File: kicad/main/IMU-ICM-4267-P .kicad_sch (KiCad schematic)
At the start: 7 parts, among them U19 ICM-42607-P

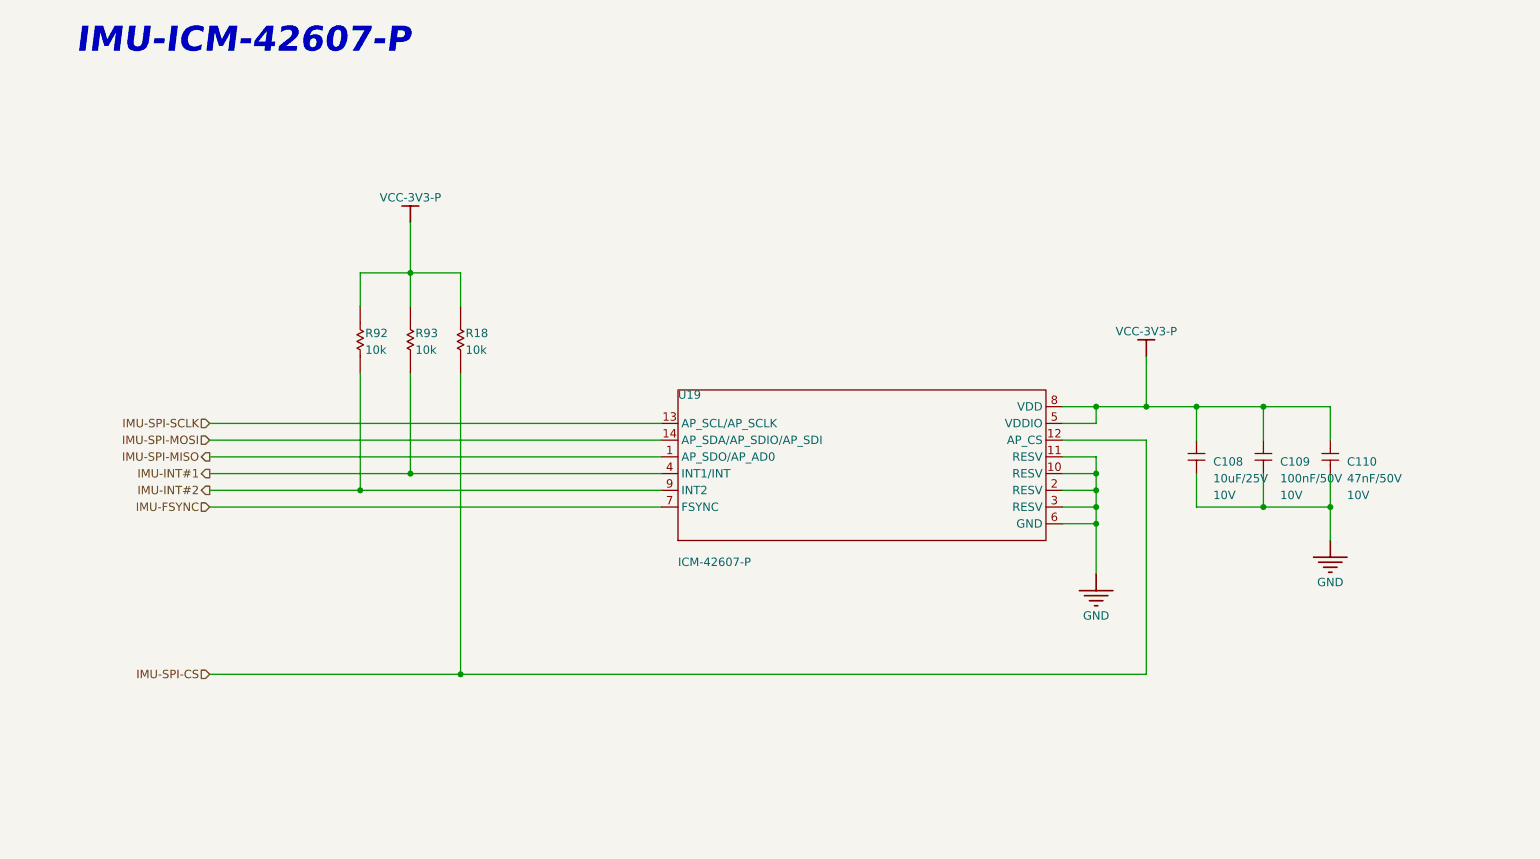
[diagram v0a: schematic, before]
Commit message: Cliff/bumpers connector
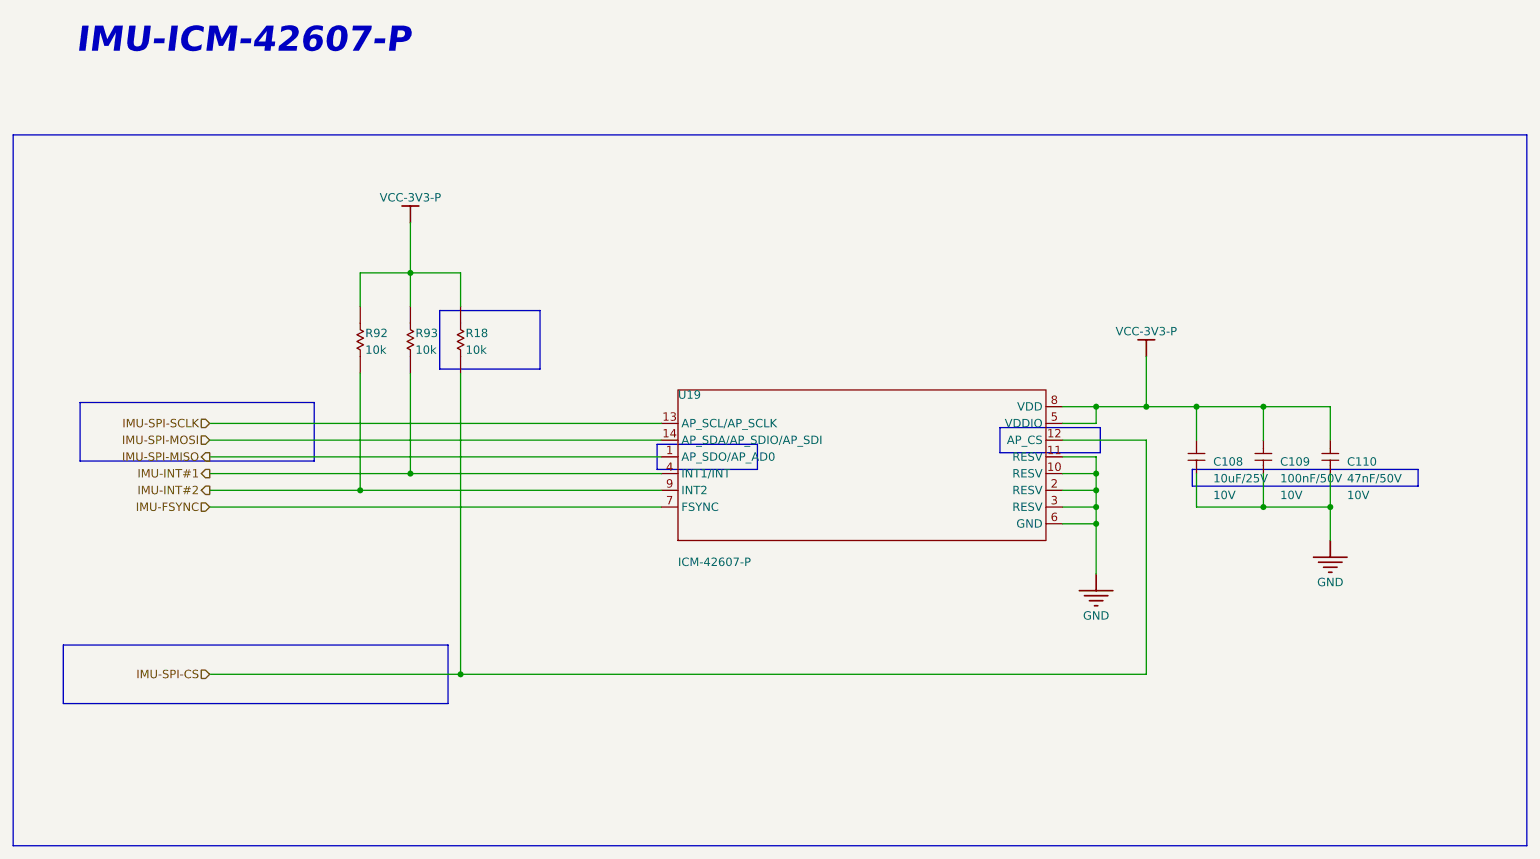
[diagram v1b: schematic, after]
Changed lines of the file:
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@@
 	(generator_version "10.0")
 	(paper "A2")
+	(rectangle
+		(start 199.39 194.31)
+		(end 234.95 203.2)
+		(stroke
+			(width 0)
+			(type solid)
+		)
+		(fill
+			(type color)
+			(color 72 0 0 1)
+		)
+	)
+	(rectangle
+		(start 196.85 231.14)
+		(end 255.27 240.03)
+		(stroke
+			(width 0)
+			(type solid)
+		)
+		(fill
+			(type color)
+			(color 72 0 0 1)
+		)
+	)
+	(rectangle
+		(start 368.3 204.47)
+		(end 402.59 207.01)
+		(stroke
+			(width 0)
+			(type solid)
+		)
+		(fill
+			(type color)
+			(color 72 0 0 1)
+		)
+	)
+	(rectangle
+		(start 339.09 198.12)
+		(end 354.33 201.93)
+		(stroke
+			(width 0)
+			(type solid)
+		)
+		(fill
+			(type color)
+			(color 72 0 0 1)
+		)
+	)
+	(rectangle
+		(start 254 180.34)
+		(end 269.24 189.23)
+		(stroke
+			(width 0)
+			(type solid)
+		)
+		(fill
+			(type color)
+			(color 72 0 0 1)
+		)
+	)
+	(rectangle
+		(start 287.02 200.66)
+		(end 302.26 204.47)
+		(stroke
+			(width 0)
+			(type solid)
+		)
+		(fill
+			(type color)
+			(color 72 0 0 1)
+		)
+	)
+	(rectangle
+		(start 189.23 153.67)
+		(end 419.1 261.62)
+		(stroke
+			(width 0)
+			(type solid)
+		)
+		(fill
+			(type color)
+			(color 0 72 0 1)
+		)
+	)
 	(text "IMU-ICM-42607-P"
 		(exclude_from_sim no)

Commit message: Second review round
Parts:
- added R72: 10k, Resistor_SMD:R_0603_1608Metric, symbol DesignLibrary:IMU_3_Resistor-1_DesignLibrary.SchLib
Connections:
- net IMU-SPI-MOSI is gone; now on net IMU-SDA: U19.14 (AP_SDA/AP_SDIO/AP_SDI)
- net VCC-3V3-P: now also U19.12 (AP_CS), R72.1
- net IMU-SPI-CS renamed IMU-SDA
- net IMU-SDA: no longer U19.12 (AP_CS)
- net IMU-SPI-MISO: no longer names the net of U19.1 (AP_SDO/AP_AD0)
- net IMU-SPI-SCLK renamed IMU-SCL
- net IMU-SCL: now also R72.2
- no-connect marks 0 -> 1

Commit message: STM32 power rail switch
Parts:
- C108: value 10uF/25V -> 10uF/6.3V; LCSC C96446 -> C1691; VOLTAGERATE 10V -> (none)
- C109: value 100nF/50V -> 100nF/6.3V; LCSC C1591 -> C5356672; VOLTAGERATE 10V -> (none)
- C110: LCSC (none) -> C1622; VOLTAGERATE 10V -> (none)
- R18, R72, R92, R93: LCSC (none) -> C98220; VOLTAGERATE * -> (none)
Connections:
- net VCC-3V3-P renamed VCC-3V3-REG
